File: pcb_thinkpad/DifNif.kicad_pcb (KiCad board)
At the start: 2 copper layers, 90 x 69 mm, 79 parts, among them J1 700C, J2 PROG, J3 SDCARD_DM3AT-SF-PEJM5, J4 HPLA_PORT, U1 ICE40HX4K-TQ144, U10 74LVC4245, U11 74LCX07, U12 74VHCT125, U13 Teensy4_1, U2 SST26VF080A-104I/SN, U3 APX803S00-29SA-7, U4 AP2114HA-3.3, U5 AP2114HA-1.2, U6 74LVC4245, U7 74LVC4245, U8 74LVC4245, U9 74LVC4245, X1 ASE-xxxMHz

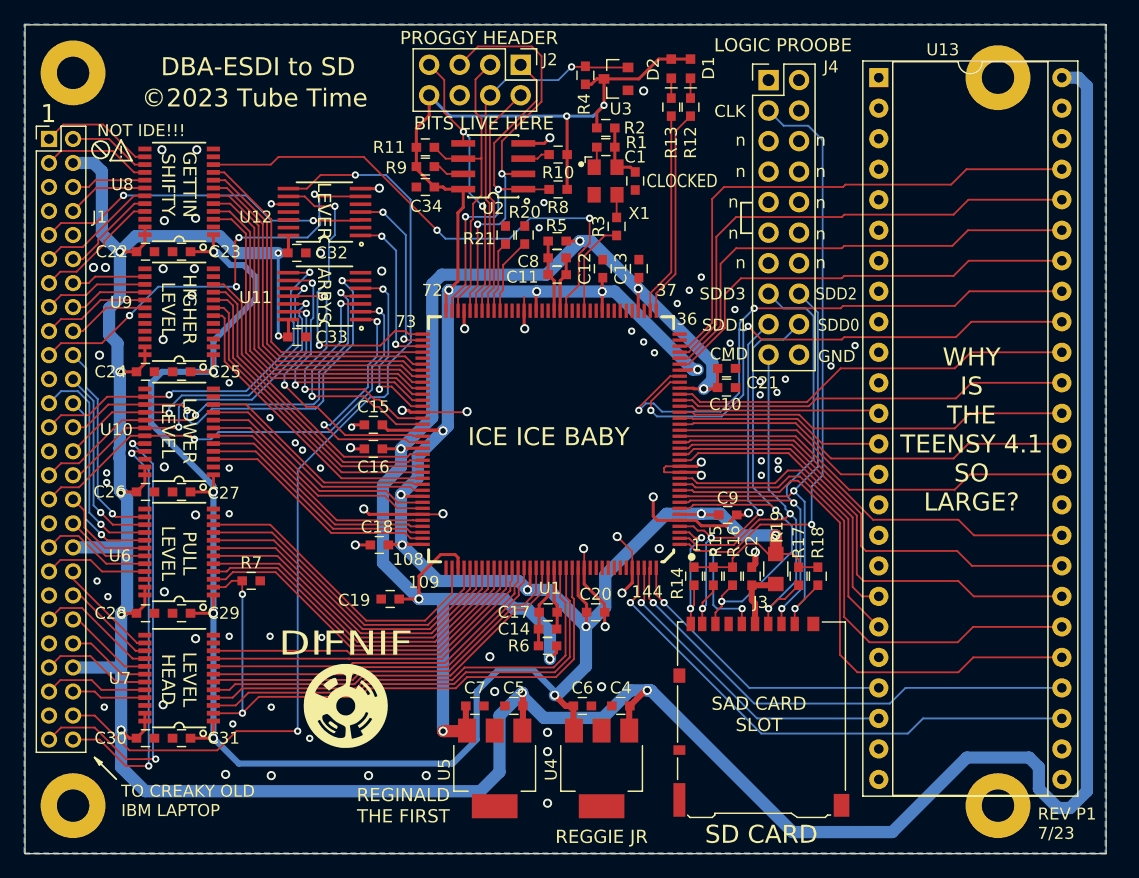
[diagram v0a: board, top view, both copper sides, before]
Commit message: Add diode OR, add clock series R
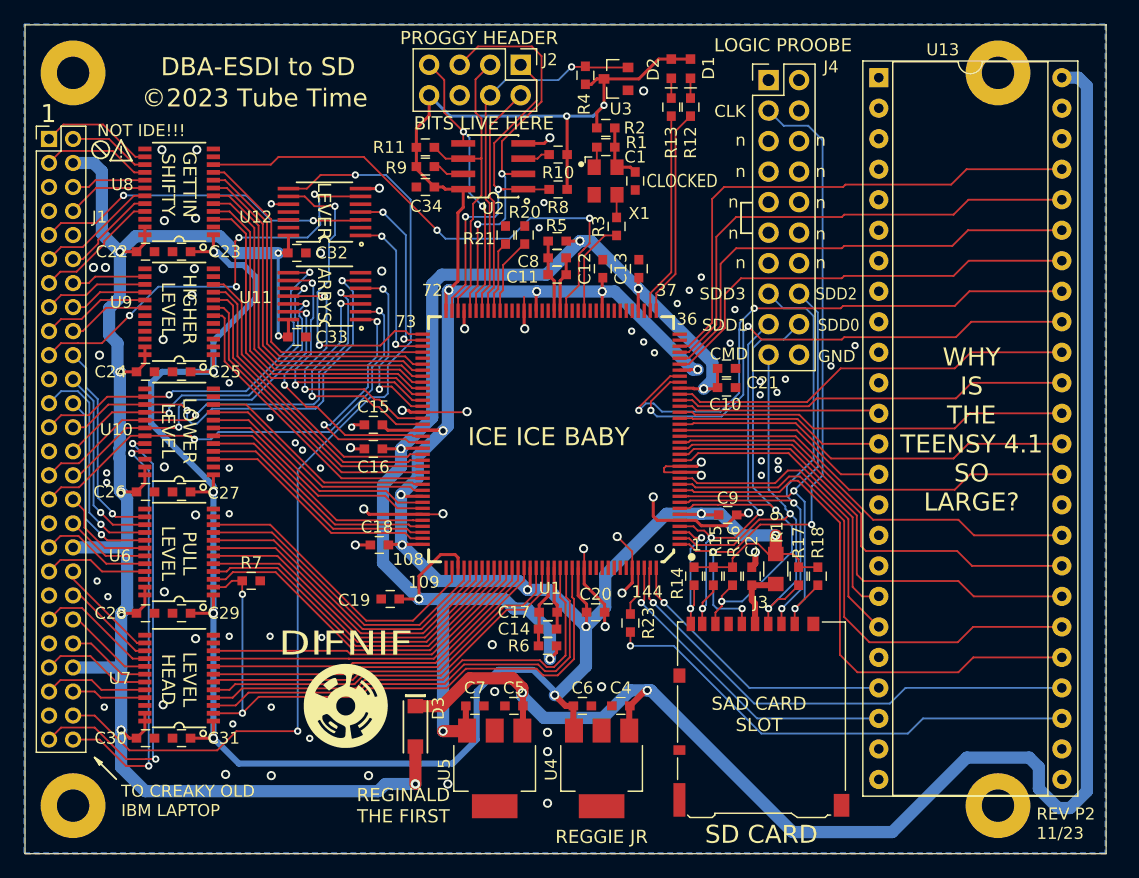
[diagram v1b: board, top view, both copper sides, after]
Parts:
- added D3: PMEG10010ELR, Active:SOD3716X117, F.Cu at (132.5, 108.4)
- added R23: 10, Passive:RESC1608X55, F.Cu at (150.4, 99.8)
- moved H4 0.40 mm to (181.0, 54.0)
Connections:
- net /DifNifBus/MADE24_5V renamed /DifNifBus/CHRESET_5V
- net /MADE24 renamed /CHRESET
- C4 pad 1: +5V -> +5VD
- C5 pad 1: +5V -> +5VD
- U1 pad 141: /TN35 -> Net-(U1-Pad141)
- U13 pad 48: +5V -> +5VD
- U4 pad 1: +5V -> +5VD
- U5 pad 1: +5V -> +5VD
- U9 pad 19: unconnected-(U9-Pad19) -> GND
- U9 pad 20: unconnected-(U9-Pad20) -> GND
- U9 pad 21: unconnected-(U9-Pad21) -> GND
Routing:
- net +5V: track 275.8 -> 136.0 mm, vias 9 -> 8
- net +5VD: track 0.00 -> 138.7 mm, vias 0 -> 2
- net Net-(U1-Pad141): track 0.00 -> 4.12 mm
- net /TN35: track 44.1 -> 40.6 mm
- net /D13: track 26.3 -> 25.7 mm
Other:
- board text added: "REV P2 11/23"
- board text removed: "REV P1 7/23"
